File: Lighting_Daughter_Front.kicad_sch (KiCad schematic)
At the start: 0 parts

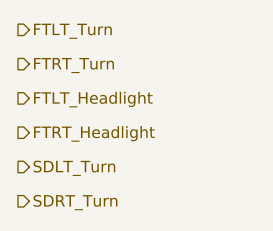
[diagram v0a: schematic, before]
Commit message: Updated Controls + Telemetry
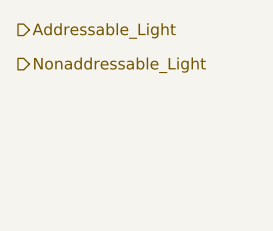
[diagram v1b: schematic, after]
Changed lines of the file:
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@@
 	(generator_version "9.0")
 	(paper "A4")
-	(hierarchical_label "FTRT_Headlight"
-		(shape output)
-		(at 127 104.14 0)
-		(effects
-			(font
-				(size 1.27 1.27)
-			)
-			(justify left)
-		)
-	)
-	(hierarchical_label "SDRT_Turn"
-		(shape output)
-		(at 127 111.76 0)
-		(effects
-			(font
-				(size 1.27 1.27)
-			)
-			(justify left)
-		)
-	)
-	(hierarchical_label "FTRT_Turn"
+	(hierarchical_label "Nonaddressable_Light"
 		(shape output)
 		(at 127 96.52 0)
@@
 		)
 	)
-	(hierarchical_label "SDLT_Turn"
-		(shape output)
-		(at 127 107.95 0)
-		(effects
-			(font
-				(size 1.27 1.27)
-			)
-			(justify left)
-		)
-	)
-	(hierarchical_label "FTLT_Headlight"
-		(shape output)
-		(at 127 100.33 0)
-		(effects
-			(font
-				(size 1.27 1.27)
-			)
-			(justify left)
-		)
-	)
-	(hierarchical_label "FTLT_Turn"
+	(hierarchical_label "Addressable_Light"
 		(shape output)
 		(at 127 92.71 0)
